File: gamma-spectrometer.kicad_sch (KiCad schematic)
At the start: 45 parts, among them J1 *, J2 *, Q1 2N7002, U1 Pico 2, U3 TLV3201AIDBVR, U4 OPA357AIDBVR, U5 OPA357AIDBVR, U6 LM4040AIM3-3.0+T, U8 MAX5026EUT_T

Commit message: ERC errors fix
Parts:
- JP1, JP2: now left out of the parts list

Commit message: Excluded from BOM
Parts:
- J1, J2: now left out of the parts list
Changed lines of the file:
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@@
 		(unit 1)
 		(exclude_from_sim no)
-		(in_bom yes)
+		(in_bom no)
 		(on_board yes)
 		(dnp no)
@@
 		(unit 1)
 		(exclude_from_sim no)
-		(in_bom yes)
+		(in_bom no)
 		(on_board yes)
 		(dnp no)

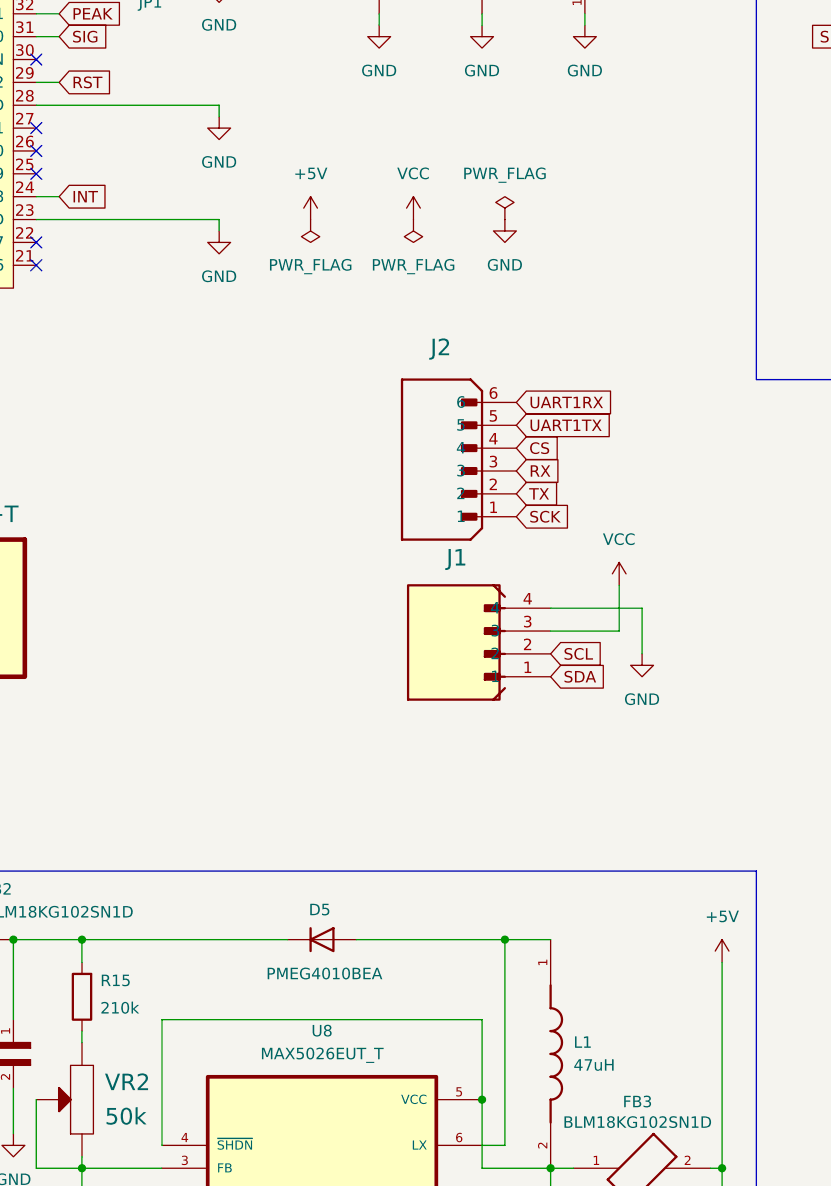
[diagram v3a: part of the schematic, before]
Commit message: Power flags fix
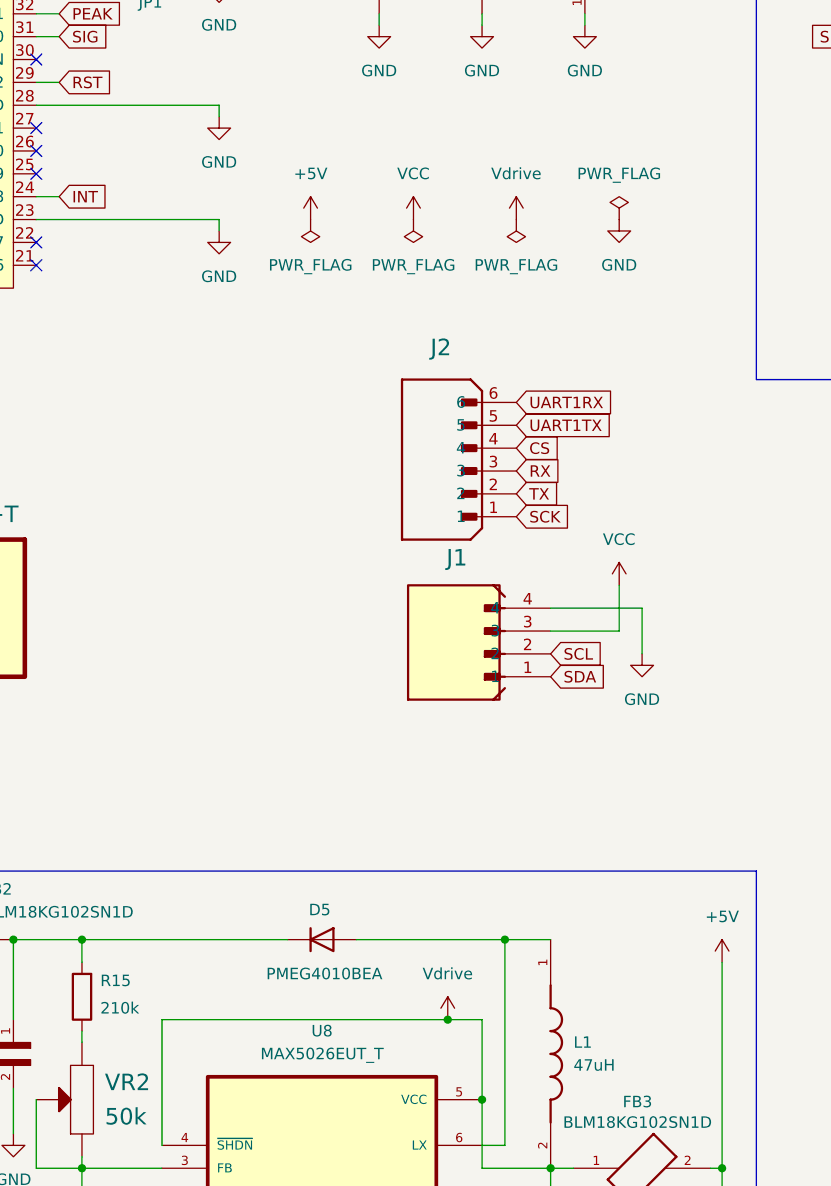
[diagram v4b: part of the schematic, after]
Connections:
- net Vdrive: now reaches C11.1, FB3.1, L1.2, U8.4 (~{SHDN}), U8.5 (VCC)
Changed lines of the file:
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@@
 	)
 	(junction
+		(at 127 156.21)
+		(diameter 0)
+		(color 0 0 0 0)
+	)
+	(junction
 		(at 86.36 172.72)
 		(diameter 0)
@@
 	(wire
 		(pts
-			(xy 95.25 156.21) (xy 130.81 156.21)
+			(xy 95.25 156.21) (xy 127 156.21)
 		)
 		(stroke
@@
 	(wire
 		(pts
+			(xy 127 156.21) (xy 130.81 156.21)
+		)
+		(stroke
+			(width 0)
+			(type default)
+		)
+	)
+	(wire
+		(pts
 			(xy 273.05 74.93) (xy 273.05 46.99)
 		)
@@
 	(symbol
 		(lib_id "power:GND")
-		(at 133.35 67.31 0)
+		(at 146.05 67.31 0)
 		(unit 1)
 		(exclude_from_sim no)
@@
 		(fields_autoplaced yes)
 		(property "Reference" "#PWR051"
-			(at 133.35 73.66 0)
+			(at 146.05 73.66 0)
 			(effects
 				(font
@@
 		)
 		(property "Value" "GND"
-			(at 133.35 72.39 0)
+			(at 146.05 72.39 0)
 			(effects
 				(font
@@
 		)
 		(property "Footprint" ""
-			(at 133.35 67.31 0)
+			(at 146.05 67.31 0)
 			(effects
 				(font
@@
 		)
 		(property "Datasheet" ""
-			(at 133.35 67.31 0)
+			(at 146.05 67.31 0)
 			(effects
 				(font
@@
 		)
 		(property "Description" "Power symbol creates a global label with name \"GND\" , ground"
-			(at 133.35 67.31 0)
+			(at 146.05 67.31 0)
 			(effects
 				(font
@@
 	)
 	(symbol
+		(lib_id "power:Vdrive")
+		(at 134.62 67.31 0)
+		(unit 1)
+		(exclude_from_sim no)
+		(in_bom yes)
+		(on_board yes)
+		(dnp no)
+		(fields_autoplaced yes)
+		(property "Reference" "#PWR072"
+			(at 134.62 71.12 0)
+			(effects
+				(font
+					(size 1.27 1.27)
+				)
+				(hide yes)
+			)
+		)
+		(property "Value" "Vdrive"
+			(at 134.62 62.23 0)
+			(effects
+				(font
+					(size 1.27 1.27)
+				)
+			)
+		)
+		(property "Footprint" ""
+			(at 134.62 67.31 0)
+			(effects
+				(font
+					(size 1.27 1.27)
+				)
+				(hide yes)
+			)
+		)
+		(property "Datasheet" ""
+			(at 134.62 67.31 0)
+			(effects
+				(font
+					(size 1.27 1.27)
+				)
+				(hide yes)
+			)
+		)
+		(property "Description" "Power symbol creates a global label with name \"Vdrive\""
+			(at 134.62 67.31 0)
+			(effects
+				(font
+					(size 1.27 1.27)
+				)
+				(hide yes)
+			)
+		)
+		(pin "1"
+		)
+		(instances
+			(project "gamma-spectrometer"
+				(path "/1fc9c372-472b-46ca-8d3b-f4aefe31a8be"
+					(reference "#PWR072")
+					(unit 1)
+				)
+			)
+		)
+	)
+	(symbol
 		(lib_id "Device:R")
 		(at 194.31 31.75 180)
@@
 	)
 	(symbol
+		(lib_id "power:Vdrive")
+		(at 127 156.21 0)
+		(unit 1)
+		(exclude_from_sim no)
+		(in_bom yes)
+		(on_board yes)
+		(dnp no)
+		(fields_autoplaced yes)
+		(property "Reference" "#PWR061"
+			(at 127 160.02 0)
+			(effects
+				(font
+					(size 1.27 1.27)
+				)
+				(hide yes)
+			)
+		)
+		(property "Value" "Vdrive"
+			(at 127 151.13 0)
+			(effects
+				(font
+					(size 1.27 1.27)
+				)
+			)
+		)
+		(property "Footprint" ""
+			(at 127 156.21 0)
+			(effects
+				(font
+					(size 1.27 1.27)
+				)
+				(hide yes)
+			)
+		)
+		(property "Datasheet" ""
+			(at 127 156.21 0)
+			(effects
+				(font
+					(size 1.27 1.27)
+				)
+				(hide yes)
+			)
+		)
+		(property "Description" "Power symbol creates a global label with name \"Vdrive\""
+			(at 127 156.21 0)
+			(effects
+				(font
+					(size 1.27 1.27)
+				)
+				(hide yes)
+			)
+		)
+		(pin "1"
+		)
+		(instances
+			(project ""
+				(path "/1fc9c372-472b-46ca-8d3b-f4aefe31a8be"
+					(reference "#PWR061")
+					(unit 1)
+				)
+			)
+		)
+	)
+	(symbol
 		(lib_id "CL10B104KC8NNNC:CL10B104KC8NNNC")
 		(at 142.24 41.91 90)
@@
 	(symbol
 		(lib_id "power:PWR_FLAG")
-		(at 133.35 67.31 0)
+		(at 146.05 67.31 0)
 		(unit 1)
 		(exclude_from_sim no)
@@
 		(fields_autoplaced yes)
 		(property "Reference" "#FLG08"
-			(at 133.35 65.405 0)
+			(at 146.05 65.405 0)
 			(effects
 				(font
@@
 		)
 		(property "Value" "PWR_FLAG"
-			(at 133.35 62.23 0)
+			(at 146.05 62.23 0)
 			(effects
 				(font
@@
 		)
 		(property "Footprint" ""
-			(at 133.35 67.31 0)
+			(at 146.05 67.31 0)
 			(effects
 				(font
@@
 		)
 		(property "Datasheet" "~"
-			(at 133.35 67.31 0)
+			(at 146.05 67.31 0)
 			(effects
 				(font
@@
 		)
 		(property "Description" "Special symbol for telling ERC where power comes from"
-			(at 133.35 67.31 0)
+			(at 146.05 67.31 0)
 			(effects
 				(font
@@
 					(unit 1)
 				)
+			)
+		)
+	)
+	(symbol
+		(lib_id "power:PWR_FLAG")
+		(at 134.62 67.31 180)
+		(unit 1)
+		(exclude_from_sim no)
+		(in_bom yes)
+		(on_board yes)
+		(dnp no)
+		(fields_autoplaced yes)
+		(property "Reference" "#FLG09"
+			(at 134.62 69.215 0)
+			(effects
+				(font
+					(size 1.27 1.27)
+				)
+				(hide yes)
+			)
+		)
+		(property "Value" "PWR_FLAG"
+			(at 134.62 72.39 0)
+			(effects
+				(font
+					(size 1.27 1.27)
+				)
+			)
+		)
+		(property "Footprint" ""
+			(at 134.62 67.31 0)
+			(effects
+				(font
+					(size 1.27 1.27)
+				)
+				(hide yes)
+			)
+		)
+		(property "Datasheet" "~"
+			(at 134.62 67.31 0)
+			(effects
+				(font
+					(size 1.27 1.27)
+				)
+				(hide yes)
+			)
+		)
+		(property "Description" "Special symbol for telling ERC where power comes from"
+			(at 134.62 67.31 0)
+			(effects
+				(font
+					(size 1.27 1.27)
+				)
+				(hide yes)
+			)
+		)
+		(pin "1"
+		)
+		(instances
+			(project "gamma-spectrometer"
+				(path "/1fc9c372-472b-46ca-8d3b-f4aefe31a8be"
+					(reference "#FLG09")
+					(unit 1)
+				)

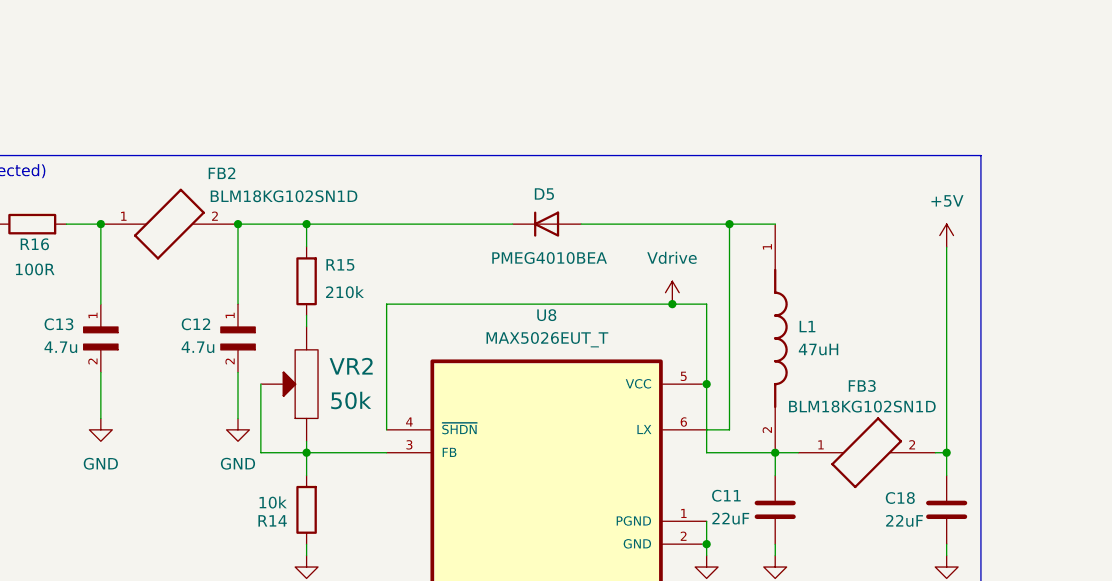
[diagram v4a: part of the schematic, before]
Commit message: C17,C19,FB1,FB2,FB3 footprint fix
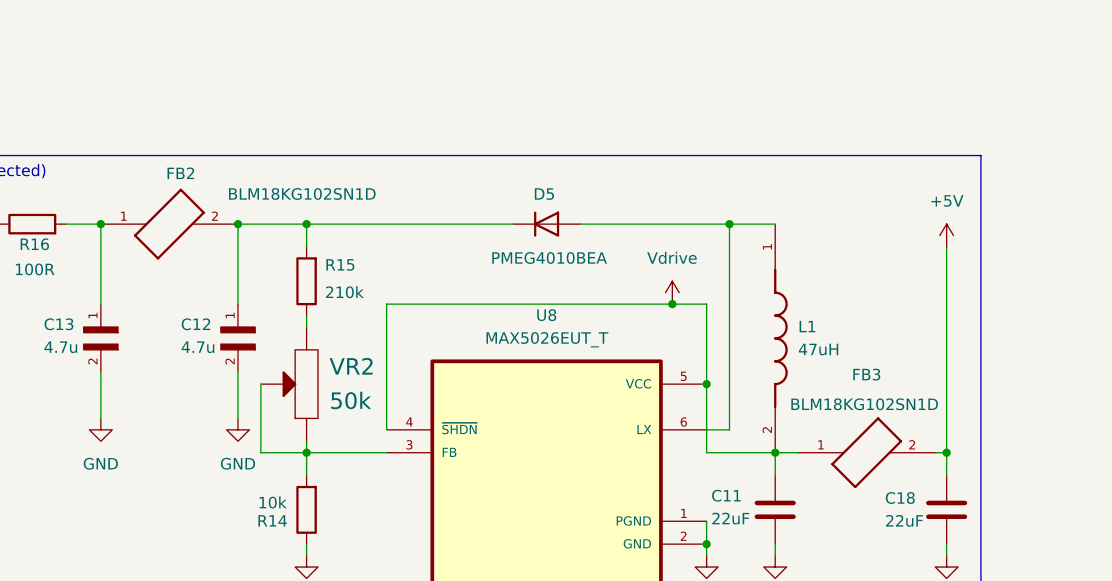
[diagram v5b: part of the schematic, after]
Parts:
- FB1, FB2, FB3: footprint ACML-0402HC-301-T:BEADC1005X65N -> BLM18KG102SN1D:BEADC1608X95N; Check_prices https://www.snapeda.com/parts/ACML-0402HC-301-T/Abracon/vie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 -> https://www.snapeda.com/parts/BLM18KG102SN1D/Murata/datashe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; Description_1 300 Ohms @ 100 MHz 1 - Ferrite Bead 0402 (1005 Metric) 1A 3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 -> 1 kOhms @ 100 MHz 1 Power Line Ferrite Bead 0603 (1608 Metr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; MF Abracon LLC -> (none); MP 490-17349-1-ND -> BLM18KG102SN1D; PACKAGE 0402 Abracon -> 0603; Package 0402 Abracon -> 0603; SnapEDA_Link https://www.snapeda.com/parts/ACML-0402HC-301-T/Abracon/vie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 -> https://www.snapeda.com/parts/BLM18KG102SN1D/Murata/datashe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
